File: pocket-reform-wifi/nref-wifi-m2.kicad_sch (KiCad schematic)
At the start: 33 parts, among them J1 Bus_M.2_Socket_E, J2 Conn_01x20, U1 TPS62A04ABDRL, X1 ECS-327MVATX-2-CN-TR3

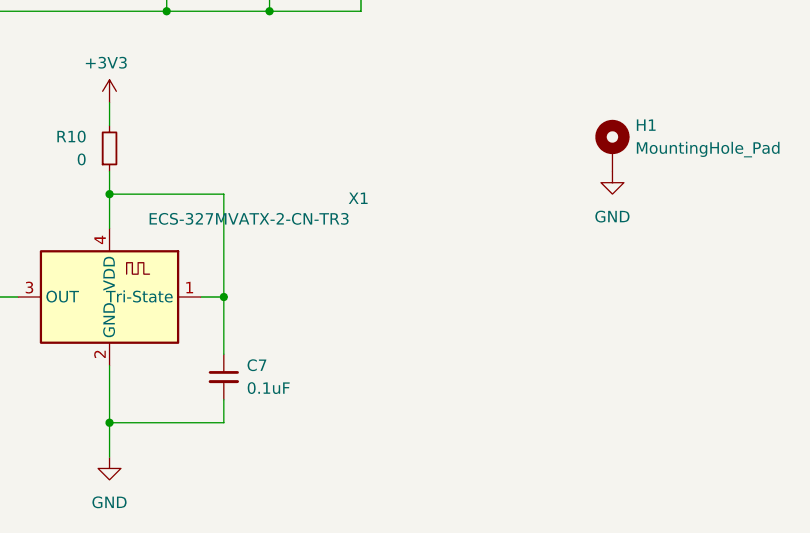
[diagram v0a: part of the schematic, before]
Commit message: m.2 wifi: component substitution
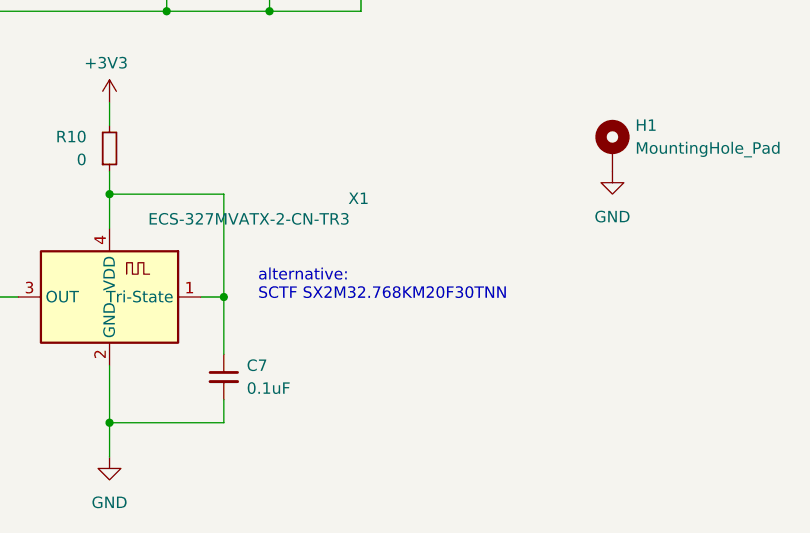
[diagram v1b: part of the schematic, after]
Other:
- note added: "alternative: SCTF SX2M32.768KM20F30TNN"
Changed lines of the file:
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@@
+		)
+	)
+	(text "alternative:\nSCTF SX2M32.768KM20F30TNN"
+		(exclude_from_sim no)
+		(at 118.11 170.18 0)
+		(effects
+			(font
+				(size 1.27 1.27)
+			)
+			(justify left)
 		)
 	)

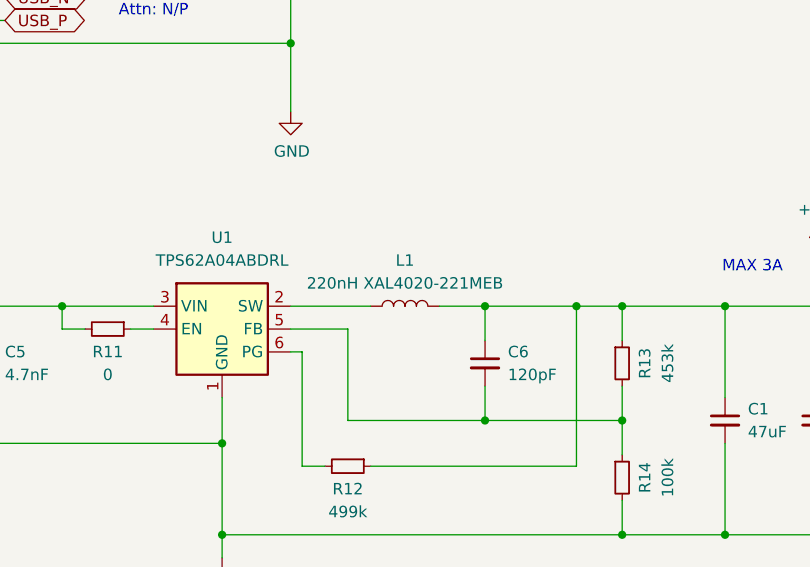
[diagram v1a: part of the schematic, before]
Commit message: pocket-reform-wifi: revision r2 with different inductor footprint
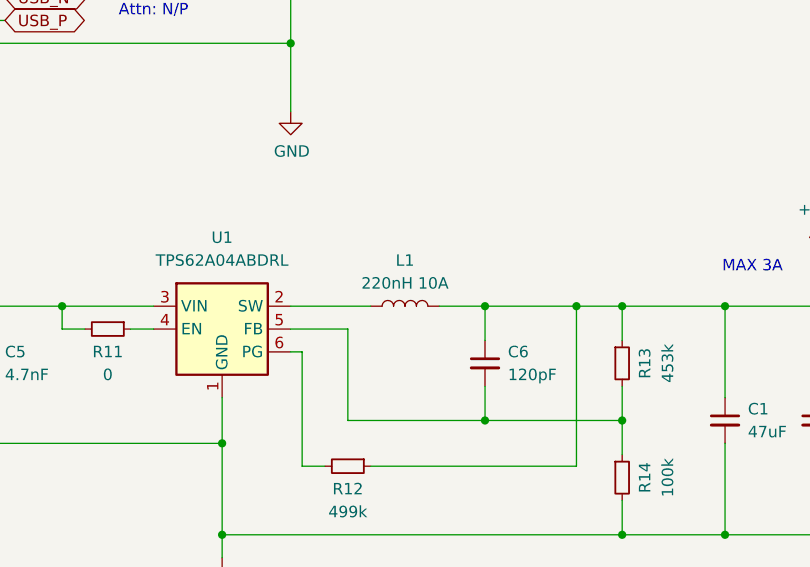
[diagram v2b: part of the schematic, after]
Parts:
- L1: value 220nH XAL4020-221MEB -> 220nH 10A; footprint Inductor_SMD:L_Coilcraft_XAL4020-XXX -> EasyEDA:IND-SMD_L3.0-W3.0_FTC303020D; LCSC C524578 -> C5832405; Manufacturer_No FXL0412-R22-M -> FTC303018DR22MBCA
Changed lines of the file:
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@@
 			)
 		)
-		(property "Value" "220nH XAL4020-221MEB"
+		(property "Value" "220nH 10A"
 			(at 83.82 111.76 90)
 			(effects
@@
 			)
 		)
-		(property "Footprint" "Inductor_SMD:L_Coilcraft_XAL4020-XXX"
+		(property "Footprint" "EasyEDA:IND-SMD_L3.0-W3.0_FTC303020D"
 			(at 83.82 114.3 0)
 			(effects
@@
 			)
 		)
-		(property "Manufacturer_No" "FXL0412-R22-M"
+		(property "Manufacturer_No" "FTC303018DR22MBCA"
 			(at 83.82 114.3 0)
 			(effects
@@
 			)
 		)
-		(property "LCSC" "C524578"
+		(property "LCSC" "C5832405"
 			(at 83.82 114.3 0)
 			(effects

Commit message: pocket-reform-wifi: revision r2 part selection tweaks for new batch
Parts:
- H1: Alt_Manufacturer Wuerth -> (none); Alt_Part_No 9774015243 -> SMTSO2015CTJ for lower height m.2 socket; LCSC C2916320 -> C2916321; Manufacturer_No SMTSO2015CTJ -> SMTSO2025CTJ; Notes (none) -> match height with m.2 socket!
- J1: Alt_Part_No (none) -> 2199119-4 (with nut SMTSO2015CTJ); LCSC global sourcing -> C41447443; Manufacturer_No 2199119-4 -> 2199230-4; Notes (none) -> original was 2199119-4, 1mm less height. match with nut hei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
- R13: LCSC C2079749 -> C25818; Manufacturer Vishay Dale -> UNI-ROYAL; Manufacturer_No CRCW0603453KFKEA -> 0603WAF4533T5E
- X1: LCSC C5375606 -> C2901603; Manufacturer ECS -> SCTF; Manufacturer_No ECS-327MVATX-2-CN-TR3 -> SX2M32.768KM20F30TNN
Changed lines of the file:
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@@
 			)
 		)
-		(property "Manufacturer_No" "2199119-4"
+		(property "Manufacturer_No" "2199230-4"
 			(at 199.39 91.44 0)
 			(effects
@@
 			)
 		)
-		(property "Notes" ""
+		(property "Notes" "original was 2199119-4, 1mm less height. match with nut height!"
 			(at 199.39 91.44 0)
 			(effects
@@
 			)
 		)
-		(property "Alt_Part_No" ""
+		(property "Alt_Part_No" "2199119-4 (with nut SMTSO2015CTJ)"
 			(at 199.39 91.44 0)
 			(effects
@@
 			)
 		)
-		(property "LCSC" "global sourcing"
+		(property "LCSC" "C41447443"
 			(at 199.39 91.44 0)
 			(effects
@@
 			)
 		)
-		(property "Manufacturer" "Vishay Dale"
+		(property "Manufacturer" "UNI-ROYAL"
 			(at 107.95 120.65 0)
 			(effects
@@
 			)
 		)
-		(property "Manufacturer_No" "CRCW0603453KFKEA"
+		(property "Manufacturer_No" "0603WAF4533T5E"
 			(at 107.95 120.65 0)
 			(effects
@@
 			)
 		)
-		(property "LCSC" "C2079749"
+		(property "LCSC" "C25818"
 			(at 107.95 120.65 0)
 			(effects
@@
 			)
 		)
-		(property "Manufacturer_No" "SMTSO2015CTJ"
+		(property "Manufacturer_No" "SMTSO2025CTJ"
 			(at 157.48 154.94 0)
 			(effects
@@
 			)
 		)
-		(property "Notes" ""
+		(property "Notes" "match height with m.2 socket!"
 			(at 157.48 154.94 0)
 			(effects
@@
 			)
 		)
-		(property "Alt_Manufacturer" "Wuerth"
+		(property "Alt_Manufacturer" ""
 			(at 157.48 154.94 0)
 			(effects
@@
 			)
 		)
-		(property "Alt_Part_No" "9774015243"
+		(property "Alt_Part_No" "SMTSO2015CTJ for lower height m.2 socket"
 			(at 157.48 154.94 0)
 			(effects
@@
 			)
 		)
-		(property "LCSC" "C2916320"
+		(property "LCSC" "C2916321"
 			(at 157.48 154.94 0)
 			(effects
@@
 			)
 		)
-		(property "Manufacturer" "ECS"
+		(property "Manufacturer" "SCTF"
 			(at 101.6 171.45 0)
 			(effects
@@
 			)
 		)
-		(property "Manufacturer_No" "ECS-327MVATX-2-CN-TR3"
+		(property "Manufacturer_No" "SX2M32.768KM20F30TNN"
 			(at 101.6 171.45 0)
 			(effects
@@
 			)
 		)
-		(property "LCSC" "C5375606"
+		(property "LCSC" "C2901603"
 			(at 101.6 171.45 0)
 			(effects
